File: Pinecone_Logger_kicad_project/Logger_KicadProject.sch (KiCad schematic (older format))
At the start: 53 parts, among them J1 Cortex_Debug_Connector_(10_pi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, U1 SAMD20G17A-A

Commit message: finished schematic design, created netlist
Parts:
- removed C? (x2): 1uF, Capacitors_SMD:C_0805, symbol C_Small
- removed C?: .1uF, Capacitors_SMD:C_0805, symbol C_Small
- removed J?: PwrJack, Lubrecht_Pcb_footprints:PJ-102a, symbol PwrJack
- removed J? (x7): 3_Pin_Term, Lubrecht_Pcb_footprints:3_Pin_Terminal, symbol 3_Pin_Term
- removed U?: MAX31856, SMD_Packages:SSOP-14, symbol MAX31856
- removed U?: SD_Micro_Slot, symbol SD_Micro_Slot
- removed U?: AP2281, TO_SOT_Packages_SMD:SOT-23-6, symbol AP2281
- removed U?: 2_Pin_Junct, symbol 2_Pin_Junct
- added C10: GRM21BR71C105KA01L, Capacitors_SMD:C_0805, symbol C_Small
- added J1: PJ-102A, Lubrecht_Pcb_footprints:PJ-102a, symbol PwrJack-RESCUE-Logger_KicadProject
- added J3: DM3AT-SF-PEJM5, Lubrecht_Pcb_footprints:hirose-dm3at, symbol SD_Micro_Slot
- added J4: OSTVN06A150, Lubrecht_Pcb_footprints:6_pin_2.54mm_term, symbol 6_pin_dht_term
- added J5: OSTVN06A150, Lubrecht_Pcb_footprints:6_pin_junction_term, symbol 6_pin_Dend_term
- added J6, J7: OSTVN06A150, Lubrecht_Pcb_footprints:6_pin_2.54mm_term, symbol 6_pin_sdi_half
- added J8: OSTVN10A150, Lubrecht_Pcb_footprints:10_pin_2.54mm_term, symbol 10_pin_tc_term
- added U6: MAX31856, Lubrecht_Pcb_footprints:TSSOP14, symbol MAX31856
- BT1: renamed from BT?; Part Id (none) -> S8201-46R
- C1, C6: renamed from C?; value 10uF -> GRM219R61A106KE44D; Capacitance (none) -> 10uF; Part Id C0805C104K5RACTU -> (none)
- C11, C13, C14, C15, C16, C17, C18, C2, C4, C5, C7, C8, C9: renamed from C?; value .1uF -> CC0603ZRY5V9BB104; Capacitance (none) -> .1uF; Part Id C0805C104K5RACTU -> (none)
- C12: renamed from C?; value .1uF -> CC0603ZRY5V9BB104; footprint 0805 -> Capacitors_SMD:C_0805; Capacitance (none) -> .1uF; Part Name Kemet C0805C104K5RACTU -> (none)
- C3: renamed from C?; value 1uF -> GRM21BR71C105KA01L; Capacitance (none) -> 1uF; Part Id C0805C104K5RACTU -> (none)
- J2: renamed from J1; value Cortex_Debug_Connector_(10_pin) -> M50-3600542
- L1: renamed from L?; value 10uH -> Z0805C221APMST; footprint (none) -> Resistors_SMD:R_0805; CD resistance (none) -> 50 mOhm
- Q2: renamed from Q?; PartId (none) -> AO3420
- R1, R3, R4, R6, R7, R8: renamed from R?; value 10K -> RC0805JR-0710KL; Resistance (none) -> 10KΩ
- R2: renamed from R?; value 10K -> RC0805JR-071KL; Resistance (none) -> 1KΩ
- R5: renamed from R?; value 10K -> RC0805JR-0710KL; Reistance (none) -> 10KΩ
- U1: footprint TQFP48 -> Housings_QFP:TQFP-48_7x7mm_Pitch0.5mm; Part Id (none) -> SAMD20G17A-A
- U2: renamed from U?; value MIC5211_Dual_Regulator -> MIC5211
- U3: renamed from U?; symbol AP2281 -> AP2281-RESCUE-Logger_KicadProject
- Y1: renamed from Y?; Part Id (none) -> MC-306 32.768K-E3:ROHS
- gave numbers to parts that had none: 5
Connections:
- net labels added: HEATER_SWITCHED_GND
- net labels removed: +5V, MAIN_SWITCHED_3v3, SD/MMC_MOSFET, SD_MOSFET, SD_SWITCHED_PWR
- wire segments 219 -> 223
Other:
- note added: "RTC, other only IC with unswitched power"
- note added: "SD socket"
- note removed: "RTC, one of only ICs with unswitched power"
- moved on the sheet: C11, C14, C15, C16, C17, C8, C9, R3, R4, R5, R6, R7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

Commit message: pcb partially done, pushing to work remotely
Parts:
- J5: footprint Lubrecht_Pcb_footprints:6_pin_junction_term -> Lubrecht_Pcb_footprints:6_pin_2.54mm_term
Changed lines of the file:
@@
 F 0 "J5" H 7300 1250 60  0000 C CNN
 F 1 "OSTVN06A150" H 7500 2100 60  0000 C CNN
-F 2 "Lubrecht_Pcb_footprints:6_pin_junction_term" H 7400 2200 60  0001 C CNN
+F 2 "Lubrecht_Pcb_footprints:6_pin_2.54mm_term" H 7400 2200 60  0001 C CNN
 F 3 "" H 7400 2200 60  0000 C CNN
 	1    7400 2200

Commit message: finished circuit design, firmware needs updating to respect pin changes
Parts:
- removed C12, C4, C5: CC0603ZRY5V9BB104, Capacitors_SMD:C_0805, symbol C_Small
- removed J1: PJ-102A, Lubrecht_Pcb_footprints:PJ-102a, symbol PwrJack-RESCUE-Logger_KicadProject
- removed J2: M50-3600542, SWD_Connector_SMD, symbol Cortex_Debug_Connector_(10_pin)
- removed J3: DM3AT-SF-PEJM5, Lubrecht_Pcb_footprints:hirose-dm3at, symbol SD_Micro_Slot
- removed J4: OSTVN06A150, Lubrecht_Pcb_footprints:6_pin_2.54mm_term, symbol 6_pin_dht_term
- removed J5: OSTVN06A150, Lubrecht_Pcb_footprints:6_pin_2.54mm_term, symbol 6_pin_Dend_term
- removed J6, J7: OSTVN06A150, Lubrecht_Pcb_footprints:6_pin_2.54mm_term, symbol 6_pin_sdi_half
- removed J8: OSTVN10A150, Lubrecht_Pcb_footprints:10_pin_2.54mm_term, symbol 10_pin_tc_term
- removed Q1, Q2, Q3, Q4: AO3420, TO_SOT_Packages_SMD:SOT-23, symbol AO3420
- removed U1: SAMD20G17A-A, Housings_QFP:TQFP-48_7x7mm_Pitch0.5mm, symbol SAMD20G17A-A
- removed U2: MIC5211, TO_SOT_Packages_SMD:SOT-23-6, symbol MIC5211_Dual_Regulator
- removed U3: AP2281, TO_SOT_Packages_SMD:SOT-23-6, symbol AP2281-RESCUE-Logger_KicadProject
- removed Y1: 32.768kHz, Lubrecht_Pcb_footprints:MC-306_Xtal, symbol Crystal_Small
- added J1: PJ-102A, Pinecone_footprints:PJ-102A, symbol PJ-102A
- added J2: M50-3600542, Pinecone_footprints:10_Pin_Cortex_SMD, symbol Cortex_SWD_Connector
- added J3: DM3AT-SF-PEJM5, Pinecone_footprints:Hirose_DM3AT, symbol SD_CARD_HOLDER_MICRO
- added J4, J5, J6, J7: OSTVN06A150, Pinecone_footprints:OSTVN06A150_6_Pin_Terminal, symbol 6_Pin_header
- added J8: 10_Pin_Header, Pinecone_footprints:OSTVN10A150_10_pin_term, symbol 10_Pin_Header
- added Q1, Q2, Q3, Q4: AO3420, TO_SOT_Packages_SMD:SOT-23, symbol BS170
- added U1: SAMD20E16A-A, Housings_QFP:TQFP-32_7x7mm_Pitch0.8mm, symbol SAMD20E16A-A
- added U2: MIC5211, TO_SOT_Packages_SMD:SOT-23-6, symbol MIC5211
- added U3: AP2281, TO_SOT_Packages_SMD:SOT-23-6, symbol AP2281
- added Y1: MC-306_32.768K-E3, Pinecone_footprints:MC-306_32.768K-E3, symbol MC-306_32.768K-E3
- BT1: footprint Lubrecht_Pcb_footprints:S8201_Bat_Holder -> Pinecone_footprints:S8201R_Batt_Holder; symbol Battery -> Battery-RESCUE-Logger_KicadProject
- C1: value GRM219R61A106KE44D -> GRM21BR71C105KA01L; Capacitance 10uF -> 1uF
- C3: value GRM21BR71C105KA01L -> GRM219R61A106KE44D; Capacitance 1uF -> 10uF
- R2: footprint Resistors_SMD:R_0805 -> R_0805
- U4: footprint Lubrecht_Pcb_footprints:SOIC-8 -> Pinecone_footprints:SOIC-8
- U5: footprint Housings_SOIC:SOIC-16_3.9x9.9mm_Pitch1.27mm -> SMD_Packages:SO-16-N
- U6: footprint Lubrecht_Pcb_footprints:TSSOP14 -> Pinecone_footprints:TSSOP-14; symbol MAX31856 -> Max31856
- renumbered C11 to C10, C13 to C11, C14 to C12, C15 to C13, C17 to C14, C16 to C15, C6 to C4, C7 to C5, C18 to C6, C9 to C7, C10 to C9
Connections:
- wire segments 223 -> 191
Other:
- moved on the sheet: C1, C11, C14, C15, C2, C3, C4, C5, C6, C7, C8, C9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

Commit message: bunch of minor changes, changed DS1302 crystal to through hole with correst ESD
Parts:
- BT1: symbol Battery-RESCUE-Logger_KicadProject -> Battery
- J1: symbol PJ-102A -> BARREL_JACK
- J2: symbol Cortex_SWD_Connector -> Cortex_Debug_Connector_(10_pin)
- J3: symbol SD_CARD_HOLDER_MICRO -> SD_Micro_Slot
- J4: symbol 6_Pin_header -> 6_pin_dht_term
- J5: symbol 6_Pin_header -> 6_pin_Dend_term
- J6, J7: symbol 6_Pin_header -> 6_pin_sdi_half
- J8: symbol 10_Pin_Header -> 10_pin_tc_term
- U2: symbol MIC5211 -> MIC5211_Dual_Regulator
- U3: symbol AP2281 -> AP2281-RESCUE-Logger_KicadProject
- U6: symbol Max31856 -> MAX31856
- Y1: value MC-306_32.768K-E3 -> CFS-20632768EZBB; footprint Pinecone_footprints:MC-306_32.768K-E3 -> Crystals:Crystal_DS26_d2.0mm_l6.0mm_Horizontal_1EP_style1; symbol MC-306_32.768K-E3 -> Crystal_Small
- renumbered L1 to FB1
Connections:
- wire segments 191 -> 196
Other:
- moved on the sheet: C11, C14, C15, C6, C7, C8, U5

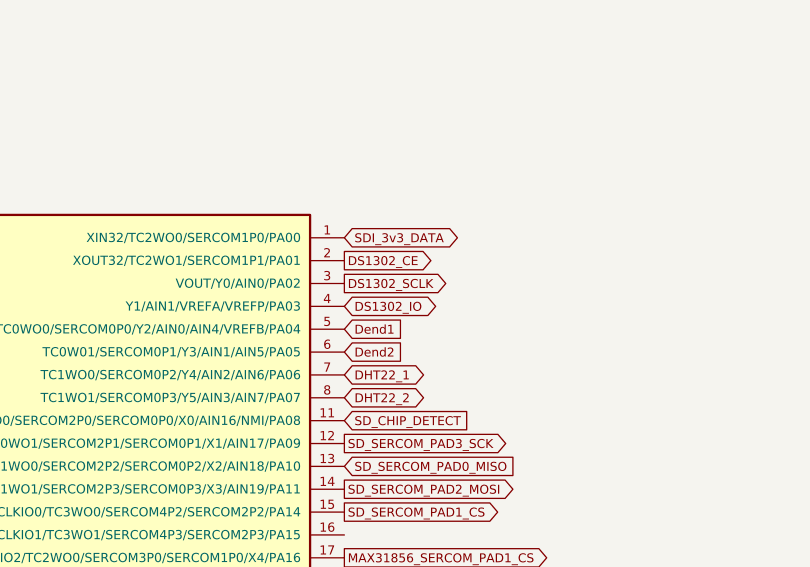
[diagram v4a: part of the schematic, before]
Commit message: completed revision of circuit design, remapped pins in conf_board
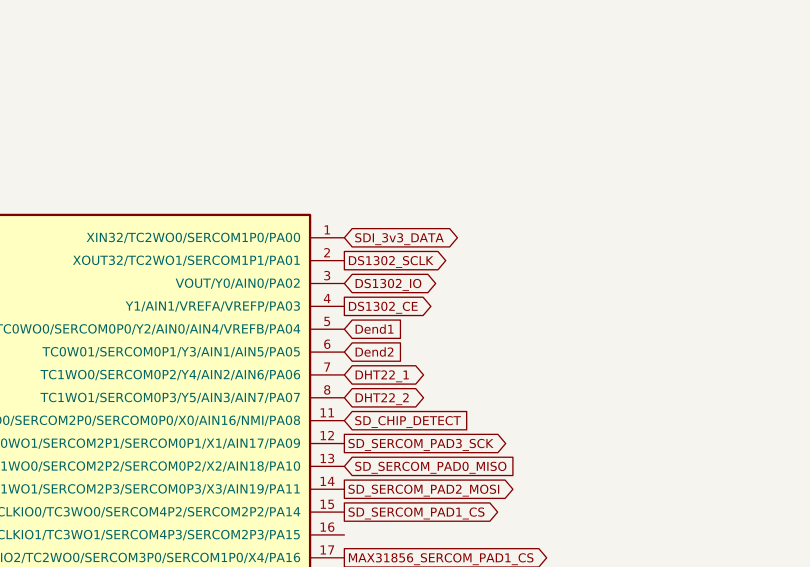
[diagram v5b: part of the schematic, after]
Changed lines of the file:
@@
 Text GLabel 13350 2550 2    39   BiDi ~ 0
 DHT22_2
-Text GLabel 13350 2050 2    39   Output ~ 0
+Text GLabel 13350 1950 2    39   Output ~ 0
 DS1302_SCLK
-Text GLabel 13350 2150 2    39   BiDi ~ 0
+Text GLabel 13350 2050 2    39   BiDi ~ 0
 DS1302_IO
-Text GLabel 13350 1950 2    39   Output ~ 0
+Text GLabel 13350 2150 2    39   Output ~ 0
 DS1302_CE
 Text GLabel 8850 5950 2    39   Output ~ 0

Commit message: changed SOT-23 MOSFETS to have correct pinout. design should work with AO3420's now
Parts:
- Q1, Q2, Q3, Q4: symbol BS170 -> BS170-RESCUE-Logger_KicadProject
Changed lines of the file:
@@
 $EndComp
 $Comp
-L BS170 Q2
+L BS170-RESCUE-Logger_KicadProject Q2
 U 1 1 586F1125
 P 3600 3700
@@
 $EndComp
 $Comp
-L BS170 Q3
+L BS170-RESCUE-Logger_KicadProject Q3
 U 1 1 586F13C8
 P 6500 3300
@@
 $EndComp
 $Comp
-L BS170 Q1
+L BS170-RESCUE-Logger_KicadProject Q1
 U 1 1 586F152B
 P 11250 8800
@@
 $EndComp
 $Comp
-L BS170 Q4
+L BS170-RESCUE-Logger_KicadProject Q4
 U 1 1 586F15E8
 P 6500 4000

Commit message: changed schematic to use DS3231
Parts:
- removed U4: DS1302, Pinecone_footprints:SOIC-8, symbol DS1302
- removed Y1: CFS-20632768EZBB, Crystals:Crystal_DS26_d2.0mm_l6.0mm_Horizontal_1EP_style1, symbol Crystal_Small
- added C16: C0805C104K5RACTU, Capacitors_SMD:C_0805, symbol C_Small
- added U?: DS3231, symbol DS3231
- C6: value CC0603ZRY5V9BB104 -> C0805C104K5RACTU
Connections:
- net labels added: DS3231_INTERRUPT, DS3231_SCL, DS3231_SDA
- net labels removed: DS1302_CE, DS1302_IO, DS1302_SCLK
- wire segments 196 -> 198
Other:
- moved on the sheet: C6
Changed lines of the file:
@@
 Text GLabel 13350 2550 2    39   BiDi ~ 0
 DHT22_2
-Text GLabel 13350 1950 2    39   Output ~ 0
-DS1302_SCLK
+Text GLabel 13350 1950 2    39   BiDi ~ 0
+DS3231_SCL
 Text GLabel 13350 2050 2    39   BiDi ~ 0
-DS1302_IO
-Text GLabel 13350 2150 2    39   Output ~ 0
-DS1302_CE
+DS3231_SDA
 Text GLabel 8850 5950 2    39   Output ~ 0
 MAX31856_SERCOM_PAD0_MISO
@@
 L Battery BT1
 U 1 1 585302CA
-P 14550 8500
-F 0 "BT1" V 14500 8200 50  0000 L CNN
-F 1 "Battery" H 14650 8450 50  0001 L CNN
-F 2 "Pinecone_footprints:S8201R_Batt_Holder" V 14550 8540 50  0001 C CNN
-F 3 "" V 14550 8540 50  0000 C CNN
-F 4 "S8201-46R" H 14550 8500 60  0001 C CNN "Part Id"
-	1    14550 8500
-	-1   0    0    1
-$EndComp
-$Comp
-L DS1302 U4
-U 1 1 5853044D
-P 14000 8600
-F 0 "U4" H 13900 8100 60  0000 C CNN
-F 1 "DS1302" H 14000 8700 60  0000 C CNN
-F 2 "Pinecone_footprints:SOIC-8" H 14000 8600 60  0001 C CNN
-F 3 "" H 14000 8600 60  0000 C CNN
-	1    14000 8600
+P 14900 8800
+F 0 "BT1" H 14950 8650 50  0000 L CNN
+F 1 "Battery" H 15000 8750 50  0001 L CNN
+F 2 "Pinecone_footprints:S8201R_Batt_Holder" V 14900 8840 50  0001 C CNN
+F 3 "" V 14900 8840 50  0000 C CNN
+F 4 "S8201-46R" H 14900 8800 60  0001 C CNN "Part Id"
+	1    14900 8800
 	1    0    0    -1
 $EndComp
@@
 Text GLabel 3950 950  2    39   Output ~ 0
 SWITCHED_3v3
-Text GLabel 14600 8800 2    39   Input ~ 0
-DS1302_SCLK
-Text GLabel 14600 8900 2    39   BiDi ~ 0
-DS1302_IO
-Text GLabel 14600 9000 2    39   Input ~ 0
-DS1302_CE
+Text GLabel 14650 8450 2    39   Input ~ 0
+DS3231_SCL
+Text GLabel 14650 8550 2    39   BiDi ~ 0
+DS3231_SDA
 Text GLabel 13350 3950 2    39   Output ~ 0
 3v3_PWR_ENABLE
@@
 L +3V3 #PWR010
 U 1 1 58597699
-P 13500 8450
-F 0 "#PWR010" H 13500 8300 50  0001 C CNN
-F 1 "+3V3" H 13500 8600 50  0000 C CNN
-F 2 "" H 13500 8450 50  0000 C CNN
-F 3 "" H 13500 8450 50  0000 C CNN
-	1    13500 8450
+P 13550 8450
+F 0 "#PWR010" H 13550 8300 50  0001 C CNN
+F 1 "+3V3" H 13550 8600 50  0000 C CNN
+F 2 "" H 13550 8450 50  0000 C CNN
+F 3 "" H 13550 8450 50  0000 C CNN
+	1    13550 8450
 	1    0    0    -1
 $EndComp
@@
 L GND #PWR011
 U 1 1 58597C9D
-P 13150 8750
-F 0 "#PWR011" H 13150 8500 50  0001 C CNN
-F 1 "GND" H 13150 8600 50  0001 C CNN
-F 2 "" H 13150 8750 50  0000 C CNN
-F 3 "" H 13150 8750 50  0000 C CNN
-	1    13150 8750
+P 13600 9200
+F 0 "#PWR011" H 13600 8950 50  0001 C CNN
+F 1 "GND" H 13600 9050 50  0001 C CNN
+F 2 "" H 13600 9200 50  0000 C CNN
+F 3 "" H 13600 9200 50  0000 C CNN
+	1    13600 9200
 	1    0    0    -1
 $EndComp
@@
 L GND #PWR012
 U 1 1 585981C8
-P 13600 9050
-F 0 "#PWR012" H 13600 8800 50  0001 C CNN
-F 1 "GND" H 13600 8900 50  0001 C CNN
-F 2 "" H 13600 9050 50  0000 C CNN
-F 3 "" H 13600 9050 50  0000 C CNN
-	1    13600 9050
+P 14700 9200
+F 0 "#PWR012" H 14700 8950 50  0001 C CNN
+F 1 "GND" H 14700 9050 50  0001 C CNN
+F 2 "" H 14700 9200 50  0000 C CNN
+F 3 "" H 14700 9200 50  0000 C CNN
+	1    14700 9200
 	1    0    0    -1
 $EndComp
@@
 L C_Small C6
 U 1 1 58599825
-P 13300 8600
-F 0 "C6" V 13400 8700 50  0000 L CNN
-F 1 "CC0603ZRY5V9BB104" V 13400 8500 50  0001 L CNN
-F 2 "Capacitors_SMD:C_0805" H 13300 8600 50  0001 C CNN
-F 3 "" H 13300 8600 50  0000 C CNN
-F 4 ".1uF" V 13250 8400 39  0000 C CNN "Capacitance"
-	1    13300 8600
-	0    1    1    0
-$EndComp
-$Comp
-L GND #PWR013
-U 1 1 58599C87
-P 14750 8550
-F 0 "#PWR013" H 14750 8300 50  0001 C CNN
-F 1 "GND" H 14750 8400 50  0001 C CNN
-F 2 "" H 14750 8550 50  0000 C CNN
-F 3 "" H 14750 8550 50  0000 C CNN
-	1    14750 8550
-	1    0    0    -1
+P 15100 8750
+F 0 "C6" H 14900 8700 50  0000 L CNN
+F 1 "C0805C104K5RACTU" V 15200 8650 50  0001 L CNN
+F 2 "Capacitors_SMD:C_0805" H 15100 8750 50  0001 C CNN
+F 3 "" H 15100 8750 50  0000 C CNN
+F 4 ".1uF" H 14950 8800 39  0000 C CNN "Capacitance"
+	1    15100 8750
+	-1   0    0    1
 $EndComp
 $Comp
@@
 Text Notes 7200 3500 0    60   ~ 0
 Ports for Dendrometers.\nData pins connected to analog inputs.
-Text Notes 14100 9300 0    60   ~ 0
+Text Notes 14050 9450 0    60   ~ 0
 RTC, other only IC with unswitched power
 $Comp
@@
 Wire Wire Line
 	13550 6400 13550 6500
-Wire Wire Line
-	13600 9000 13600 9050
 Connection ~ 3700 3950
 Wire Wire Line
@@
 Wire Wire Line
 	3700 3900 3700 4000
-Wire Wire Line
-	14500 9000 14600 9000
-Wire Wire Line
-	14600 8900 14500 8900
-Wire Wire Line
-	14500 8800 14600 8800
 Wire Wire Line
 	6700 5750 6850 5750
@@
 	10000 2500 10000 2450
 Wire Wire Line
-	14550 8700 14500 8700
-Wire Wire Line
 	13400 6400 13600 6400
 Connection ~ 13550 6400
@@
 Wire Wire Line
 	7750 6350 7750 6300
-$Comp
-L Crystal_Small Y1
-U 1 1 587475EE
-P 13400 8850
-F 0 "Y1" H 13350 8350 60  0000 C CNN
-F 1 "CFS-20632768EZBB" H 13550 8200 60  0000 C CNN
-F 2 "Crystals:Crystal_DS26_d2.0mm_l6.0mm_Horizontal_1EP_style1" H 13400 8850 60  0001 C CNN
-F 3 "" H 13400 8850 60  0001 C CNN
-	1    13400 8850
-	0    1    1    0
-$EndComp
 $Comp
 L R_Small R2
@@
 	10450 6200 10450 6300
 Wire Wire Line
-	13600 8800 13500 8800
-Wire Wire Line
-	13500 8800 13500 8750
-Wire Wire Line
-	13500 8750 13400 8750
-Wire Wire Line
-	13600 8900 13500 8900
-Wire Wire Line
-	13500 8900 13500 8950
-Wire Wire Line
-	13500 8950 13400 8950
-Wire Wire Line
-	13500 8700 13600 8700
-Wire Wire Line
-	13500 8450 13500 8700
-Wire Wire Line
 	5750 900  5800 900
 Wire Wire Line
@@
 Wire Wire Line
 	10000 2750 10850 2750
-Wire Wire Line
-	13500 8600 13400 8600
-Connection ~ 13500 8600
-Wire Wire Line
-	13200 8600 13150 8600
-Wire Wire Line
-	13150 8600 13150 8750
-Wire Wire Line
-	14550 8700 14550 8650
-Wire Wire Line
-	14550 8350 14750 8350
-Wire Wire Line
-	14750 8350 14750 8550
 Text GLabel 8950 6300 2    39   Input ~ 0
 SWITCHED_3v3
@@
 Wire Wire Line
 	7550 6050 7550 6150
+$Comp
+L DS3231 U?
+U 1 1 58B0BC60
+P 14000 8350
+F 0 "U?" H 13900 7350 60  0000 C CNN
+F 1 "DS3231" H 14250 8450 60  0000 C CNN
+F 2 "" H 14000 8350 60  0000 C CNN
+F 3 "" H 14000 8350 60  0000 C CNN
+	1    14000 8350
+	1    0    0    -1
+$EndComp
+Wire Wire Line
+	14600 8650 15100 8650
+$Comp
+L C_Small C16
+U 1 1 58B0D767
+P 13450 8800
+F 0 "C16" H 13300 8700 50  0000 L CNN
+F 1 "C0805C104K5RACTU" V 13550 8700 50  0001 L CNN
+F 2 "Capacitors_SMD:C_0805" H 13450 8800 50  0001 C CNN
+F 3 "" H 13450 8800 50  0000 C CNN
+F 4 ".1uF" H 13300 8800 39  0000 C CNN "Capacitance"
+	1    13450 8800
+	1    0    0    -1
+$EndComp
+Connection ~ 14900 8650
+$Comp
+L GND #PWR?
+U 1 1 58B0E284
+P 15100 8900
+F 0 "#PWR?" H 15100 8650 50  0001 C CNN
+F 1 "GND" H 15100 8750 50  0001 C CNN
+F 2 "" H 15100 8900 50  0000 C CNN
+F 3 "" H 15100 8900 50  0000 C CNN
+	1    15100 8900
+	1    0    0    -1
+$EndComp
+Wire Wire Line
+	14650 8550 14600 8550
+Wire Wire Line
+	14600 8450 14650 8450
+Text GLabel 13350 2150 2    39   Input ~ 0
+DS3231_INTERRUPT
+Text GLabel 13300 8650 0    39   Output ~ 0
+DS3231_INTERRUPT
+Wire Wire Line
+	13450 8550 13650 8550
+Wire Wire Line
+	13550 8550 13550 8450
+Wire Wire Line
+	13550 8850 13650 8850
+Wire Wire Line
+	13450 8950 13650 8950
+Wire Wire Line
+	13550 9050 13650 9050
+Connection ~ 13550 8950
+Wire Wire Line
+	13550 9150 13650 9150
+Connection ~ 13550 9050
+Wire Wire Line
+	13600 9150 13600 9200
+Connection ~ 13600 9150
+Wire Wire Line
+	14600 8750 14700 8750
+Wire Wire Line
+	14700 8750 14700 9200
+Wire Wire Line
+	14700 8850 14600 8850
+Wire Wire Line
+	14600 8950 14900 8950
+Connection ~ 14700 8850
+Wire Wire Line
+	14700 9050 14600 9050
+Connection ~ 14700 8950
+Wire Wire Line
+	14700 9150 14600 9150
+Connection ~ 14700 9050
+Connection ~ 14700 9150
+Wire Wire Line
+	15100 8900 15100 8850
+Wire Wire Line
+	13650 8650 13300 8650
+Wire Wire Line
+	13450 8550 13450 8700
+Connection ~ 13550 8550
+Wire Wire Line
+	13550 8850 13550 9150
+Wire Wire Line
+	13450 8900 13450 8950
 $EndSCHEMATC

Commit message: added MAX3231 to board, changed xlator mosfets to work
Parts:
- removed C6: C0805C104K5RACTU, Capacitors_SMD:C_0805, symbol C_Small
- removed Q3, Q4: AO3420, TO_SOT_Packages_SMD:SOT-23, symbol BS170-RESCUE-Logger_KicadProject
- added R9: RC0805JR-0710KL, Resistors_SMD:R_0805, symbol R_Small
- BT1: symbol Battery -> Battery-RESCUE-Logger_KicadProject
- C10, C11, C12, C13, C14, C15, C2, C5, C7, C8: value CC0603ZRY5V9BB104 -> C0805C104K5RACTU
- J1: symbol BARREL_JACK -> BARREL_JACK-RESCUE-Logger_KicadProject
- U4: renamed from U?; footprint (none) -> Housings_SOIC:SOIC-16W_7.5x10.3mm_Pitch1.27mm
- renumbered C16 to C6
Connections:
- wire segments 198 -> 194
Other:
- moved on the sheet: R5, R6
